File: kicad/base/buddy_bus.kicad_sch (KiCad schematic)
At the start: 32 parts, among them J10 Conn_01x06_Socket, J11 Conn_01x06_Socket, J12 Conn_01x06_Socket, J13 Conn_01x06_Socket, J14 Conn_01x06_Socket, J15 Conn_01x06_Socket, J16 Conn_01x06_Socket, J17 Conn_01x06_Socket, J3 Conn_01x06_Socket, J4 Conn_01x06_Socket, J5 Conn_01x06_Socket, J6 Conn_01x06_Socket, J7 Conn_01x06_Socket, J8 Conn_01x06_Socket, J9 Conn_01x06_Socket, U2 THVD1450DR

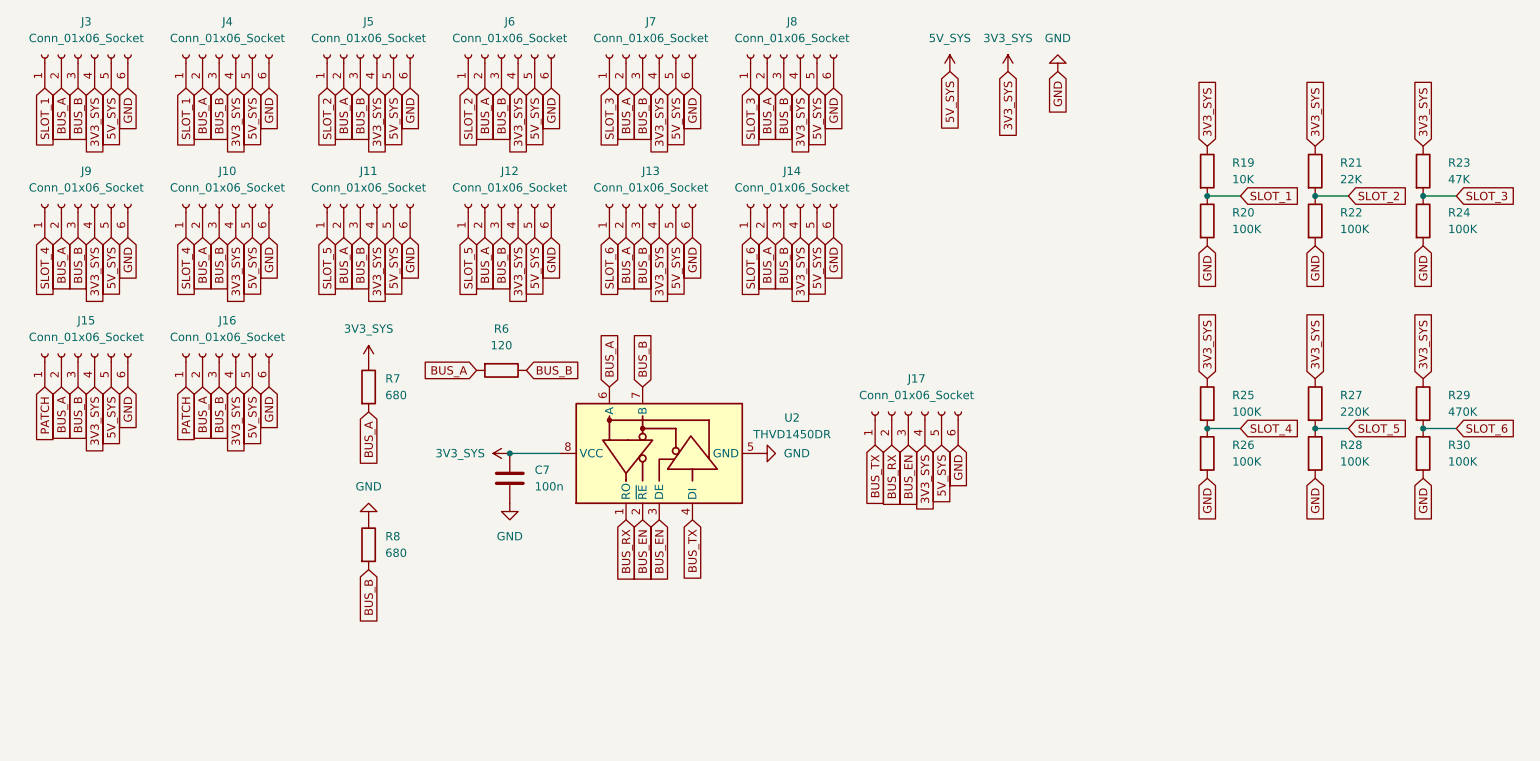
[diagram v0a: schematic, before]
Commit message: Add Buddy Audio bus
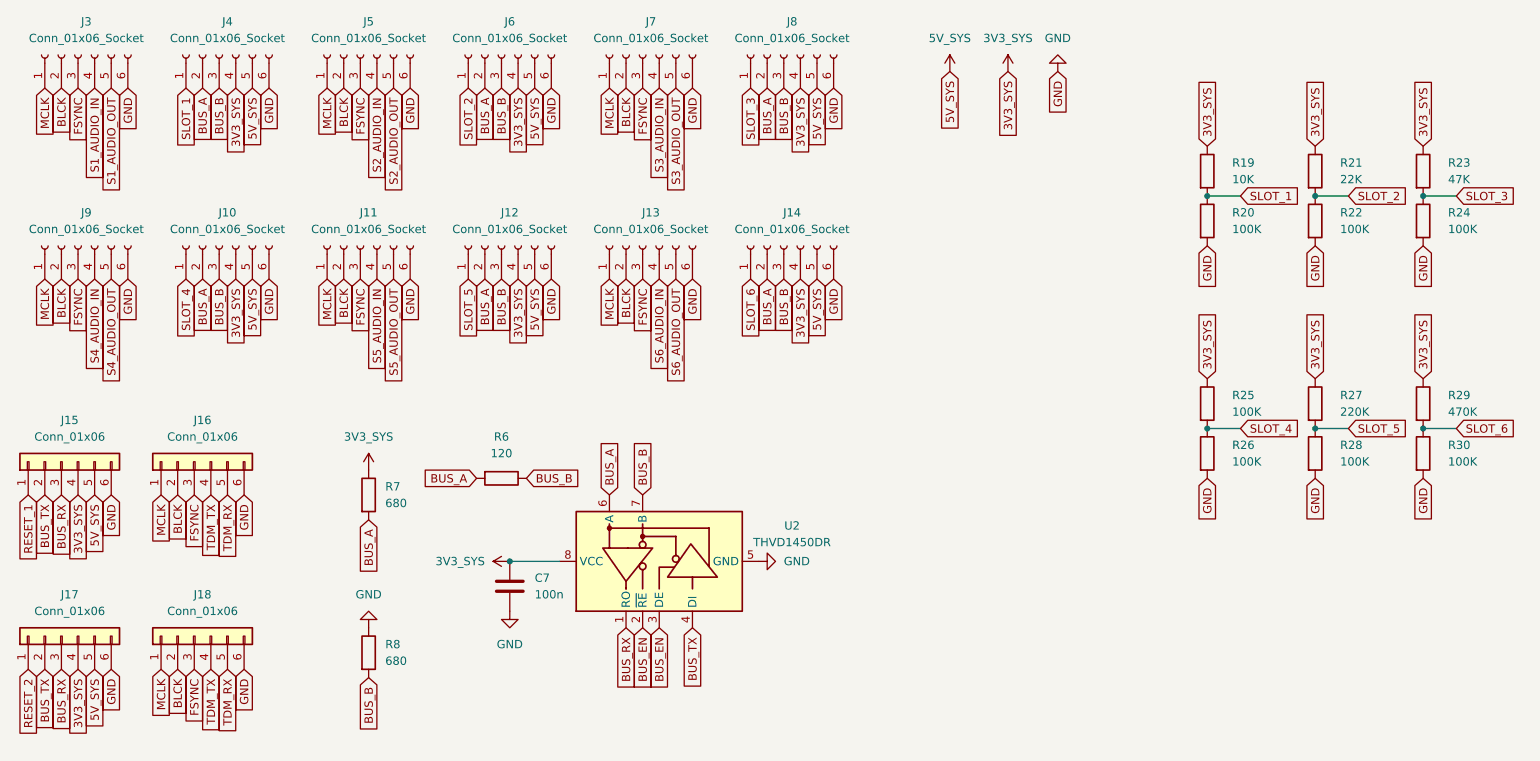
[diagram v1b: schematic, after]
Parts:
- removed J15, J16, J17: Conn_01x06_Socket, Connector_PinSocket_2.54mm:PinSocket_1x06_P2.54mm_Vertical, symbol Connector:Conn_01x06_Socket
- added J15, J16, J17, J18: Conn_01x06, Connector_PinSocket_2.54mm:PinSocket_1x06_P2.54mm_Vertical, symbol Connector_Generic:Conn_01x06
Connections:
- net 3V3_SYS: now also J15.4 (Pin_4), J17.4 (Pin_4); no longer J11.4 (Pin_4), J13.4 (Pin_4), J3.4 (Pin_4), J5.4 (Pin_4), J7.4 (Pin_4), J9.4 (Pin_4)
- net 5V_SYS: now also J15.5 (Pin_5), J17.5 (Pin_5); no longer J11.5 (Pin_5), J13.5 (Pin_5), J3.5 (Pin_5), J5.5 (Pin_5), J7.5 (Pin_5), J9.5 (Pin_5)
- net BUS_A: no longer J11.2 (Pin_2), J13.2 (Pin_2), J3.2 (Pin_2), J5.2 (Pin_2), J7.2 (Pin_2), J9.2 (Pin_2)
- net BUS_B: no longer J11.3 (Pin_3), J13.3 (Pin_3), J3.3 (Pin_3), J5.3 (Pin_3), J7.3 (Pin_3), J9.3 (Pin_3)
- net BUS_RX: now also J15.3 (Pin_3), J17.3 (Pin_3)
- net BUS_TX: now also J15.2 (Pin_2), J17.2 (Pin_2)
- net GND: now also J15.6 (Pin_6), J16.6 (Pin_6), J17.6 (Pin_6), J18.6 (Pin_6)
- net SLOT_1: no longer J3.1 (Pin_1)
- net SLOT_2: no longer J5.1 (Pin_1)
- net SLOT_3: no longer J7.1 (Pin_1)
- net SLOT_4: no longer J9.1 (Pin_1)
- net SLOT_5: no longer J11.1 (Pin_1)
- net SLOT_6: no longer J13.1 (Pin_1)
- new net BLCK: J11.2 (Pin_2), J13.2 (Pin_2), J16.2 (Pin_2), J18.2 (Pin_2), J3.2 (Pin_2), J5.2 (Pin_2), J7.2 (Pin_2), J9.2 (Pin_2)
- new net FSYNC: J11.3 (Pin_3), J13.3 (Pin_3), J16.3 (Pin_3), J18.3 (Pin_3), J3.3 (Pin_3), J5.3 (Pin_3), J7.3 (Pin_3), J9.3 (Pin_3)
- new net MCLK: J11.1 (Pin_1), J13.1 (Pin_1), J16.1 (Pin_1), J18.1 (Pin_1), J3.1 (Pin_1), J5.1 (Pin_1), J7.1 (Pin_1), J9.1 (Pin_1)
- new net RESET_1: J15.1 (Pin_1)
- new net RESET_2: J17.1 (Pin_1)
- new net S1_AUDIO_IN: J3.4 (Pin_4)
- new net S1_AUDIO_OUT: J3.5 (Pin_5)
- new net S2_AUDIO_IN: J5.4 (Pin_4)
- new net S2_AUDIO_OUT: J5.5 (Pin_5)
- new net S3_AUDIO_IN: J7.4 (Pin_4)
- new net S3_AUDIO_OUT: J7.5 (Pin_5)
- new net S4_AUDIO_IN: J9.4 (Pin_4)
- new net S4_AUDIO_OUT: J9.5 (Pin_5)
- new net S5_AUDIO_IN: J11.4 (Pin_4)
- new net S5_AUDIO_OUT: J11.5 (Pin_5)
- new net S6_AUDIO_IN: J13.4 (Pin_4)
- new net S6_AUDIO_OUT: J13.5 (Pin_5)
- new net TDM_RX: J16.5 (Pin_5), J18.5 (Pin_5)
- new net TDM_TX: J16.4 (Pin_4), J18.4 (Pin_4)
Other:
- moved on the sheet: C7, J10, J11, J12, J13, J14, J9, R6, R7, R8, U2
